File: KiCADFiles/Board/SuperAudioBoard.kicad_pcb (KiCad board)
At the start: 4 copper layers, 88.9 x 68.6 mm, 288 parts, among them K301 CONN_3, K302 CONN_3, K303 CONN_3, K304 CONN_3, K801 CONN_3, M3_HOLE VAL**, P801 CONN_2, U201 TEENSY_3_1, U202 SI8662BC, U203 SI8602AC, U301 CS4272, U302 OPA2348, U401 THS4521, U501 THS4521, U601 THS4521, U701 THS4521, U801 BAT4XAA, U802 LT1962-3.3, U803 LT1962-5, U804 LTC3534, X301 CRYSTAL

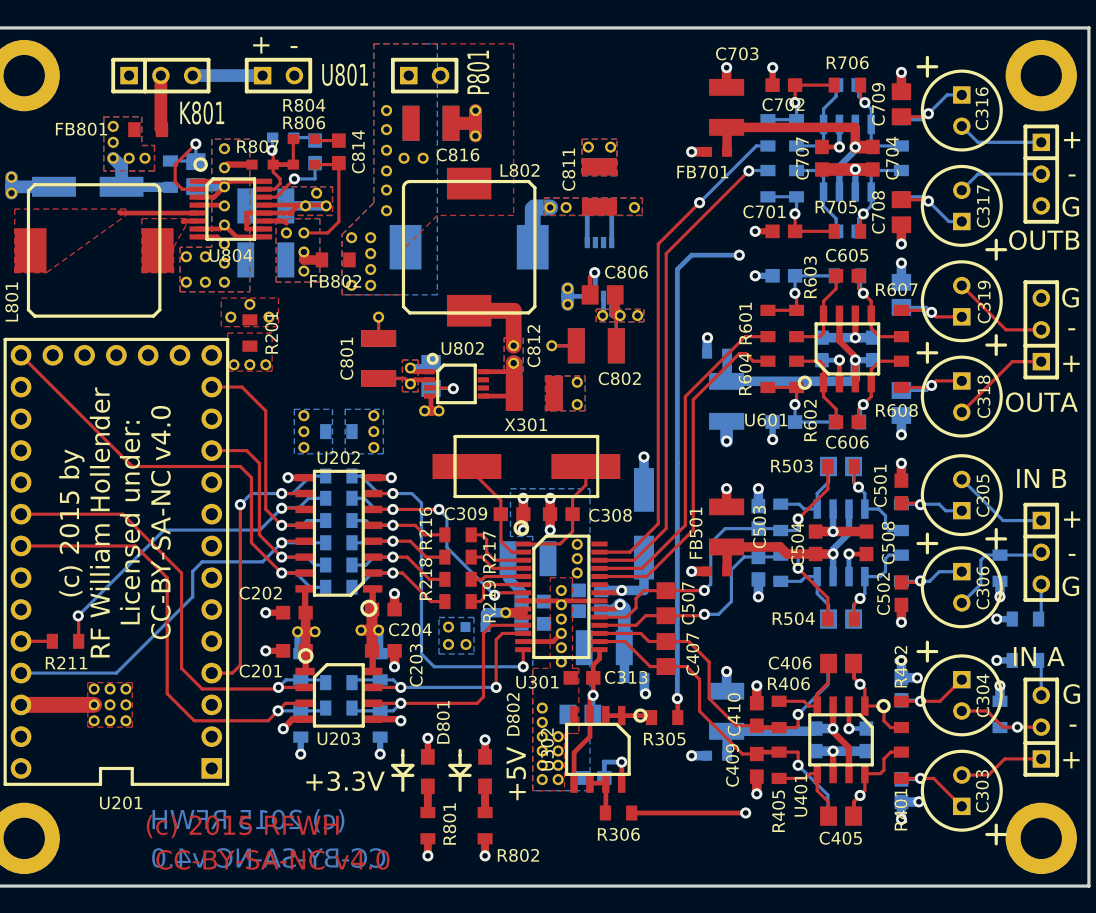
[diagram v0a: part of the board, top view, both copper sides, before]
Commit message: initial schematic with RPI pico
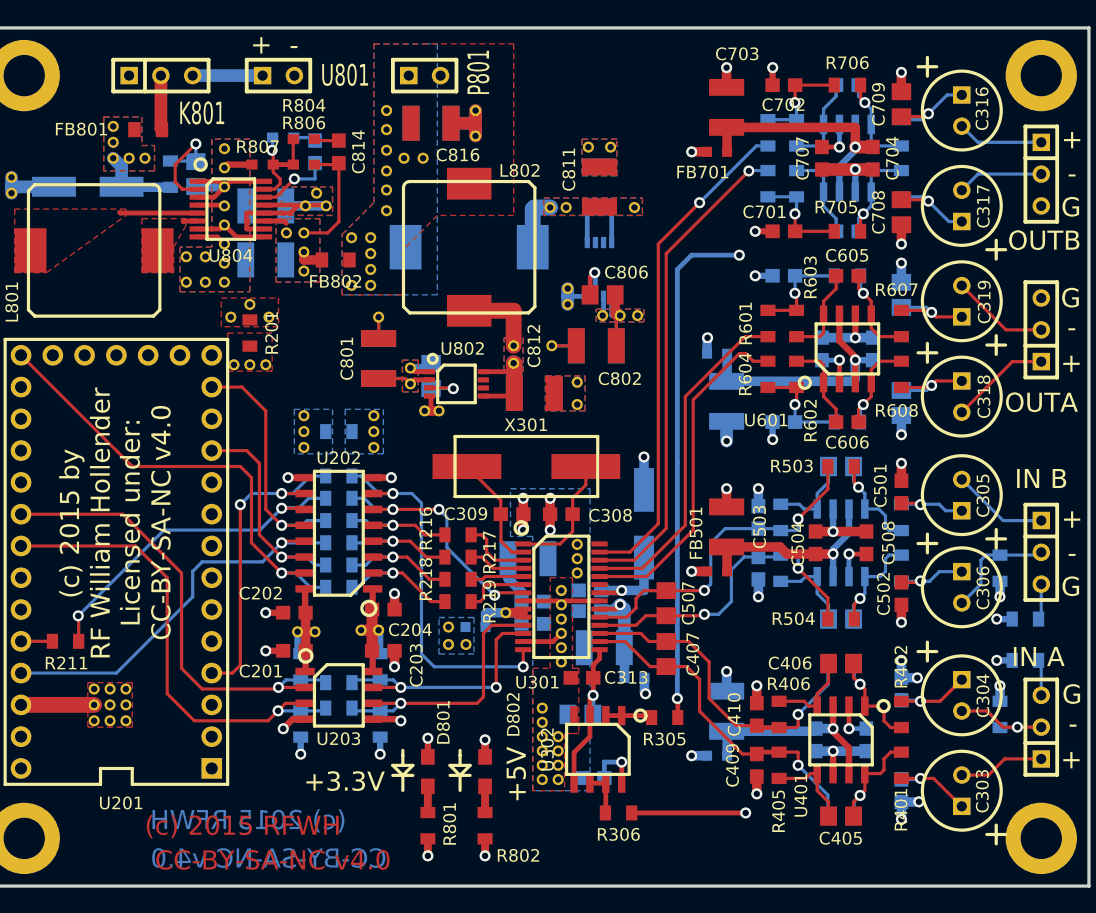
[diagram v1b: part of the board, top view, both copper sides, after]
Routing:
- added copper zone on In2.Cu, net +3.3V
- added copper zone on In2.Cu, net +5VA
- added copper zone on In2.Cu, net /TeensyAndDigital/T_3.3V
- added copper zone on In2.Cu, net /TeensyAndDigital/T_VIN
- added copper zone on In2.Cu, net /TeensyAndDigital/VUSB
- added copper zone on In1.Cu, net DGND
- added copper zone on In1.Cu, net GND
- added copper zone on In2.Cu, net GND
- added copper zone on In2.Cu, net N-00000104
- removed copper zone on Inner1.Cu, net +3.3V
- removed copper zone on Inner1.Cu, net +5VA
- removed copper zone on Inner1.Cu, net /TeensyAndDigital/T_3.3V
- removed copper zone on Inner1.Cu, net /TeensyAndDigital/T_VIN
- removed copper zone on Inner1.Cu, net /TeensyAndDigital/VUSB
- removed copper zone on Inner2.Cu, net DGND
- removed copper zone on Inner1.Cu, net GND
- removed copper zone on Inner2.Cu, net GND
- removed copper zone on Inner1.Cu, net N-00000104
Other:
- net class Default removed
- net class Thick1 removed
- net class Thick2 removed
- net class Thick3 removed
- net class Thick4 removed
- net class Thick5 removed

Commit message: chose all components
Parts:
- removed C201, C202, C203, C204, C301, C307, C312, C313, C314, C320, C404, C408, C504, C508, C604, C607, C704, C707: 0.1u, Kemet_0603
- removed C302, C310, C403, C503, C603, C703, C801, C802, C803, C804, C808, C810, C811, C812, C813, C816, C817: 10uF, Kemet_1210
- removed C303, C304, C305, C306, C316, C317, C318, C319: 100u, Nichicon_UFW_6_3mm
- removed C308, C309: 39p, Kemet_0603
- removed C311: 1u, Kemet_0805
- removed C315, C807: 47uF, Elec_cap_47u
- removed C401, C402, C409, C410, C501, C502, C509, C510: 100p, Kemet_0603
- removed C405, C406, C505, C506: 1n, Kemet_0805
- removed C407, C507: 2.7n, Kemet_0805
- removed C601, C602, C701, C702: 1.3nF, Kemet_0603
- removed C605, C606, C705, C706: 300pF, Kemet_0603
- removed C608, C609, C708, C709: 33nF, Kemet_0805
- removed C805, C806: 0.01uF, Kemet_0805
- removed C809: 0.056uF, Kemet_0805
- removed C814: 33pF, Kemet_0603
- removed C815: 330pF, Kemet_0603
- removed C818: 22uF, Kemet_1210
- removed D801, D802: LED, LED_0805
- removed FB301, FB302, FB401, FB501, FB601, FB701: 220, Bead_0603
- removed FB801, FB802: 330R, Bead_0805
- removed K301, K302, K303, K304, K801: CONN_3, SIL-3
- removed L801, L802, L803: 5.2uH, MSS1038
- removed M3_HOLE (x4): VAL**, M3_HOLE
- removed P801: CONN_2, SIL-2
- removed R201, R202, R203, R204, R205, R206, R207, R208, R209, R210, R301, R302, R303, R304: 0, Yageo_0805
- removed R211, R216, R217, R218, R219: 51, Yageo_0805
- removed R212, R213, R214, R215: 2.2K, Yageo_0805
- removed R305, R306: 10, Yageo_0805
- removed R401, R402, R403, R404, R501, R502, R503, R504: 1k, Yageo_0805
- removed R405, R406, R505, R506: 40.2, Yageo_0805
- removed R601, R602, R603, R604, R605, R606, R701, R702, R703, R704, R705, R706: 5.1K, Yageo_0805
- removed R607, R608, R707, R708: 100, Yageo_0805
- removed R801: 270, Yageo_0805
- removed R802: 620, Yageo_0805
- removed R803: 200k, Yageo_0805
- removed R804: 10k, Yageo_0603
- removed R805: 15k, Yageo_0603
- removed R806: 649k, Yageo_0603
- removed R807: 137k, Yageo_0603
- removed STITCHING_VIA (x111): VAL**, STITCHING_VIA
- removed U201: TEENSY_3_1, TEENSY_3_1
- removed U202: SI8662BC, SILABS_N_SOIC_16
- removed U203: SI8602AC, SILABS_N_SOIC_8
- removed U301: CS4272, INF_TSSOP_28
- removed U302: OPA2348, TI_SOIC8
- removed U401, U501, U601, U701: THS4521, TI_SOIC8
- removed U801: BAT4XAA, SIL-2
- removed U802: LT1962-3.3, LINEAR_MS8
- removed U803: LT1962-5, LINEAR_MS8
- removed U804: LTC3534, LINEAR_SSOP_16_N
- removed X301: CRYSTAL, XTAL
- added C14: 2200p, PCM_SparkFun-Capacitor:C_0603_1608Metric, F.Cu at (203.3, 136.5)
- added C15: 470p, PCM_SparkFun-Capacitor:C_0603_1608Metric, F.Cu at (129.9, 139.2)
- added C18: 100u, Capacitor_THT:CP_Radial_D5.0mm_P2.00mm, F.Cu at (161.1, 80.1)
- added C21: 100u, Capacitor_THT:CP_Radial_D5.0mm_P2.00mm, F.Cu at (161.1, 86.7)
- added C23: 100u, Capacitor_THT:CP_Radial_D5.0mm_P2.00mm, F.Cu at (161.1, 93.2)
- added C24: 470p, PCM_SparkFun-Capacitor:C_0603_1608Metric, F.Cu at (217.1, 103.1)
- added C34: 100u, Capacitor_THT:CP_Radial_D5.0mm_P2.00mm, F.Cu at (161.1, 99.8)
- added C39: 470p, PCM_SparkFun-Capacitor:C_0603_1608Metric, F.Cu at (217.1, 105.6)
- added C40: 0.1u, PCM_SparkFun-Capacitor:C_0603_1608Metric, F.Cu at (217.1, 108.1)
- added C41: 470p, PCM_SparkFun-Capacitor:C_0603_1608Metric, F.Cu at (203.3, 139.1)
- added C42: 1500p, PCM_SparkFun-Capacitor:C_0603_1608Metric, F.Cu at (129.9, 141.7)
- added C45: 1500p, PCM_SparkFun-Capacitor:C_0603_1608Metric, F.Cu at (203.3, 141.6)
- added C46: 22u, Capacitor_THT:CP_Radial_D5.0mm_P2.00mm, F.Cu at (134.2, 145.3)
- added C47: 22u, Capacitor_THT:CP_Radial_D5.0mm_P2.00mm, F.Cu at (207.7, 145.1)
- added C48: 6.8n, PCM_SparkFun-Capacitor:C_0603_1608Metric, F.Cu at (129.9, 144.2)
- added C49: 6.8n, PCM_SparkFun-Capacitor:C_0603_1608Metric, F.Cu at (203.3, 144.1)
- added C50: 10u, PCM_SparkFun-Capacitor:C_0805_2012Metric, F.Cu at (134.1, 150.1)
- added C51: 0.1u, PCM_SparkFun-Capacitor:C_0603_1608Metric, F.Cu at (129.9, 146.8)
- added C54: 10u, PCM_SparkFun-Capacitor:C_0805_2012Metric, F.Cu at (207.5, 149.9)
- added C55: 0.1u, PCM_SparkFun-Capacitor:C_0603_1608Metric, F.Cu at (203.3, 146.6)
- added C56: 100u, Capacitor_THT:CP_Radial_D5.0mm_P2.00mm, F.Cu at (161.1, 106.3)
- added C7: 100u, Capacitor_THT:CP_Radial_D5.0mm_P2.00mm, F.Cu at (211.7, 121.6)
- added C80: 0.1u, PCM_SparkFun-Capacitor:C_0603_1608Metric, F.Cu at (178.3, 132.3)
- added C81: 1n, PCM_SparkFun-Capacitor:C_0603_1608Metric, F.Cu at (178.3, 134.8)
- added C82: 1n, PCM_SparkFun-Capacitor:C_0603_1608Metric, F.Cu at (178.3, 137.3)
- added C85: 5800p, PCM_SparkFun-Capacitor:C_0603_1608Metric, F.Cu at (178.3, 139.8)
- added C86: 5800p, PCM_SparkFun-Capacitor:C_0603_1608Metric, F.Cu at (178.3, 142.3)
- added C9: 2200p, PCM_SparkFun-Capacitor:C_0603_1608Metric, F.Cu at (129.9, 136.7)
- added C90: 0.1u, PCM_SparkFun-Capacitor:C_0603_1608Metric, F.Cu at (211.1, 68.5)
- added C91: 1n, PCM_SparkFun-Capacitor:C_0603_1608Metric, F.Cu at (211.1, 71.0)
- added C92: 1n, PCM_SparkFun-Capacitor:C_0603_1608Metric, F.Cu at (211.1, 73.5)
- added C95: 5800p, PCM_SparkFun-Capacitor:C_0603_1608Metric, F.Cu at (211.1, 76.0)
- added C96: 5800p, PCM_SparkFun-Capacitor:C_0603_1608Metric, F.Cu at (211.1, 78.5)
- added FB7: 220, Inductor_SMD:L_0603_1608Metric, F.Cu at (129.9, 149.3)
- added FB8: 220, Inductor_SMD:L_0603_1608Metric, F.Cu at (203.3, 149.1)
- added J1: NCJ5FI-H, Connector_Audio:Jack_XLR-6.35mm_Neutrik_NCJ5FI-H_Horizontal, F.Cu at (167.8, 56.2)
- added J2: NRJ4HF, Connector_Audio:Jack_6.35mm_Neutrik_NRJ4HF_Horizontal, F.Cu at (131.8, 50.9)
- added J3: Barrel_Jack_PTH, PCM_SparkFun-Connector:Barrel_Jack_PTH, F.Cu at (202.0, 127.9)
- added J4: NRJ4HF, Connector_Audio:Jack_6.35mm_Neutrik_NRJ4HF_Horizontal, F.Cu at (131.8, 68.7)
- added J5: NRJ4HF, Connector_Audio:Jack_6.35mm_Neutrik_NRJ4HF_Horizontal, F.Cu at (131.8, 86.5)
- added R10: 5, PCM_SparkFun-Resistor:R_0805_2012Metric, F.Cu at (225.5, 89.8)
- added R11: 1k, PCM_SparkFun-Resistor:R_0805_2012Metric, F.Cu at (225.5, 92.7)
- added R12: 100, PCM_SparkFun-Resistor:R_0805_2012Metric, F.Cu at (167.5, 81.3)
- added R14: 1k, PCM_SparkFun-Resistor:R_0805_2012Metric, F.Cu at (165.6, 116.0)
- added R15: 1k, PCM_SparkFun-Resistor:R_0805_2012Metric, F.Cu at (198.5, 52.2)
- added R16: 39k, PCM_SparkFun-Resistor:R_0805_2012Metric, F.Cu at (225.5, 95.7)
- added R17: 1k, PCM_SparkFun-Resistor:R_0805_2012Metric, F.Cu at (225.5, 98.6)
- added R18: 4.42k, PCM_SparkFun-Resistor:R_0805_2012Metric, F.Cu at (125.7, 136.9)
- added R19: 4.42k, PCM_SparkFun-Resistor:R_0805_2012Metric, F.Cu at (199.1, 136.8)
- added R20: 1.33k, PCM_SparkFun-Resistor:R_0805_2012Metric, F.Cu at (125.7, 139.9)
- added R21: 1.33k, PCM_SparkFun-Resistor:R_0805_2012Metric, F.Cu at (199.1, 139.7)
- added R22: 2.32k, PCM_SparkFun-Resistor:R_0805_2012Metric, F.Cu at (125.7, 142.8)
- added R23: 715, PCM_SparkFun-Resistor:R_0805_2012Metric, F.Cu at (125.7, 145.8)
- added R24: 2.32k, PCM_SparkFun-Resistor:R_0805_2012Metric, F.Cu at (199.1, 142.7)
- added R25: 715, PCM_SparkFun-Resistor:R_0805_2012Metric, F.Cu at (199.1, 145.6)
- added R26: 4.99k, PCM_SparkFun-Resistor:R_0805_2012Metric, F.Cu at (125.7, 148.7)
- added R27: 4.99k, PCM_SparkFun-Resistor:R_0805_2012Metric, F.Cu at (199.1, 148.6)
- added R28: 1.5k, PCM_SparkFun-Resistor:R_0805_2012Metric, F.Cu at (125.7, 151.7)
- added R29: 1.5k, PCM_SparkFun-Resistor:R_0805_2012Metric, F.Cu at (199.1, 151.5)
- added R3: 39k, PCM_SparkFun-Resistor:R_0805_2012Metric, F.Cu at (211.6, 126.3)
- added R30: 100, PCM_SparkFun-Resistor:R_0805_2012Metric, F.Cu at (167.5, 84.2)
- added R31: 100, PCM_SparkFun-Resistor:R_0805_2012Metric, F.Cu at (167.5, 87.2)
- added R32: 47k, PCM_SparkFun-Resistor:R_0805_2012Metric, F.Cu at (167.5, 90.1)
- added R33: 47k, PCM_SparkFun-Resistor:R_0805_2012Metric, F.Cu at (167.5, 93.1)
- added R34: 100, PCM_SparkFun-Resistor:R_0805_2012Metric, F.Cu at (167.5, 96.0)
- added R35: 0, PCM_SparkFun-Resistor:R_0805_2012Metric, F.Cu at (125.7, 132.0)
- added R4: 3.3k, PCM_SparkFun-Resistor:R_0805_2012Metric, F.Cu at (211.6, 129.3)
- added R5: 39k, PCM_SparkFun-Resistor:R_0805_2012Metric, F.Cu at (167.5, 78.3)
- added R6: 34, PCM_SparkFun-Resistor:R_0805_2012Metric, F.Cu at (225.5, 83.9)
- added R65: 10k, PCM_SparkFun-Resistor:R_0805_2012Metric, F.Cu at (165.6, 119.0)
- added R67: 1k, PCM_SparkFun-Resistor:R_0805_2012Metric, F.Cu at (165.6, 121.9)
- added R69: 1k, PCM_SparkFun-Resistor:R_0805_2012Metric, F.Cu at (165.6, 124.9)
- added R7: 39k, PCM_SparkFun-Resistor:R_0805_2012Metric, F.Cu at (225.5, 86.8)
- added R70: 34, PCM_SparkFun-Resistor:R_0805_2012Metric, F.Cu at (165.6, 127.8)
- added R71: 34, PCM_SparkFun-Resistor:R_0805_2012Metric, F.Cu at (165.6, 130.8)
- added R74: 10k, PCM_SparkFun-Resistor:R_0805_2012Metric, F.Cu at (198.5, 55.2)
- added R76: 1k, PCM_SparkFun-Resistor:R_0805_2012Metric, F.Cu at (198.5, 58.1)
- added R78: 1k, PCM_SparkFun-Resistor:R_0805_2012Metric, F.Cu at (198.5, 61.1)
- added R79: 34, PCM_SparkFun-Resistor:R_0805_2012Metric, F.Cu at (198.5, 64.0)
- added R8: 500, PCM_SparkFun-Resistor:R_0805_2012Metric, F.Cu at (165.6, 113.1)
- added R80: 34, PCM_SparkFun-Resistor:R_0805_2012Metric, F.Cu at (198.5, 67.0)
- added R9: 500, PCM_SparkFun-Resistor:R_0805_2012Metric, F.Cu at (198.5, 49.3)
- added RV3: 5k, Potentiometer_THT:Potentiometer_Alps_RK163_Single_Horizontal, F.Cu at (215.8, 87.1)
- added RV4: 5k, Potentiometer_THT:Potentiometer_Alps_RK163_Single_Horizontal, F.Cu at (187.4, 116.3)
- added RV5: 5k, Potentiometer_THT:Potentiometer_Alps_RK163_Single_Horizontal, F.Cu at (220.2, 52.5)
- added SW4: ~, Connector_PinHeader_2.54mm:PinHeader_1x03_P2.54mm_Horizontal, F.Cu at (178.2, 79.1)
- added TP1: TestPoint_2Pole, TestPoint:TestPoint_2Pads_Pitch2.54mm_Drill0.8mm, F.Cu at (211.2, 113.3)
- added TP2: TestPoint_2Pole, TestPoint:TestPoint_2Pads_Pitch2.54mm_Drill0.8mm, F.Cu at (211.2, 116.6)
- added TP3: TestPoint_2Pole, TestPoint:TestPoint_2Pads_Pitch2.54mm_Drill0.8mm, F.Cu at (171.6, 78.5)
- added TP4: TestPoint_2Pole, TestPoint:TestPoint_2Pads_Pitch2.54mm_Drill0.8mm, F.Cu at (171.6, 81.9)
- added TP5: TestPoint_2Pole, TestPoint:TestPoint_2Pads_Pitch2.54mm_Drill0.8mm, F.Cu at (171.6, 85.2)
- added TP6: TestPoint_2Pole, TestPoint:TestPoint_2Pads_Pitch2.54mm_Drill0.8mm, F.Cu at (171.6, 88.6)
- added U1: OPA1655D, Package_SO:SOIC-8_3.9x4.9mm_P1.27mm, F.Cu at (136.1, 138.8)
- added U10: OPA1655D, Package_SO:SOIC-8_3.9x4.9mm_P1.27mm, F.Cu at (210.8, 105.2)
- added U15: OPA1655D, Package_SO:SOIC-8_3.9x4.9mm_P1.27mm, F.Cu at (172.1, 134.4)
- added U16: OPA1655D, Package_SO:SOIC-8_3.9x4.9mm_P1.27mm, F.Cu at (172.1, 141.0)
- added U17: OPA1655D, Package_SO:SOIC-8_3.9x4.9mm_P1.27mm, F.Cu at (204.9, 70.6)
- added U18: OPA1655D, Package_SO:SOIC-8_3.9x4.9mm_P1.27mm, F.Cu at (204.9, 77.2)
- added U4: OPA1655D, Package_SO:SOIC-8_3.9x4.9mm_P1.27mm, F.Cu at (209.5, 138.6)
- added U6: 1512S08-U, Package_SO:SOIC-8_5.3x5.3mm_P1.27mm, F.Cu at (201.4, 105.4)
- added U7: Teensy4.0, Teensy:Teensy40, F.Cu at (143.1, 121.0)
- added U8: LT1962, Package_SO:MSOP-8_3x3mm_P0.65mm, F.Cu at (200.6, 131.0)
- added U9: OPA1655D, Package_SO:SOIC-8_3.9x4.9mm_P1.27mm, F.Cu at (174.0, 93.6)
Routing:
- net GND: track 135.0 -> 0.00 mm, vias 41 -> 0
- net /CodecAndAnalog/OutputBufferA/VCOM: track 72.7 -> 0.00 mm, vias 4 -> 0
- net /CodecAndAnalog/InputBufferA/VCOM: track 58.0 -> 0.00 mm, vias 3 -> 0
- net /CodecAndAnalog/OutputBufferB/IN_N: track 40.0 -> 0.00 mm, vias 1 -> 0
- net /CodecAndAnalog/OutputBufferB/IN_P: track 39.2 -> 0.00 mm, vias 1 -> 0
- net /TeensyAndDigital/T_SCL: track 38.4 -> 0.00 mm, vias 1 -> 0
- net /TeensyAndDigital/T_SDA: track 37.1 -> 0.00 mm, vias 1 -> 0
- net /TeensyAndDigital/T_ADC_DATA: track 37.0 -> 0.00 mm, vias 1 -> 0
- net /TeensyAndDigital/T_LRCLK: track 31.8 -> 0.00 mm, vias 1 -> 0
- net /TeensyAndDigital/RSTN: track 30.0 -> 0.00 mm, vias 2 -> 0
- net /TeensyAndDigital/T_DAC_DATA: track 27.6 -> 0.00 mm, vias 2 -> 0
- net /CodecAndAnalog/InputBufferB/OUT_N: track 27.3 -> 0.00 mm, vias 2 -> 0
- net /CodecAndAnalog/InputBufferA/OUT_N: track 27.2 -> 0.00 mm, vias 1 -> 0
- net /CodecAndAnalog/OutputBufferA/IN_N: track 27.2 -> 0.00 mm
- net /CodecAndAnalog/OutputBufferA/IN_P: track 27.2 -> 0.00 mm
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- removed copper zone on B.Cu, net +3.3V
- removed copper zone on F.Cu, net +3.3V
- removed copper zone on In2.Cu, net +3.3V
- removed copper zone on B.Cu, net +5VA
- removed copper zone on F.Cu, net +5VA
- removed copper zone on In2.Cu, net +5VA
- removed copper zone on F.Cu, net /TeensyAndDigital/T_3.3V
- removed copper zone on In2.Cu, net /TeensyAndDigital/T_3.3V
- removed copper zone on F.Cu, net /TeensyAndDigital/T_VIN
- removed copper zone on In2.Cu, net /TeensyAndDigital/T_VIN
- removed copper zone on F.Cu, net /TeensyAndDigital/VUSB
- removed copper zone on In2.Cu, net /TeensyAndDigital/VUSB
- removed copper zone on B.Cu, net DGND
- removed copper zone on In1.Cu, net DGND
- removed copper zone on B.Cu, net GND
- removed copper zone on F.Cu, net GND
- removed copper zone on In1.Cu, net GND
- removed copper zone on In2.Cu, net GND
- removed copper zone on B.Cu, net N-00000101
- removed copper zone on F.Cu, net N-00000101
- removed copper zone on B.Cu, net N-00000104
- removed copper zone on F.Cu, net N-00000104
- removed copper zone on In2.Cu, net N-00000104
- removed copper zone on F.Cu, net N-00000107
- removed copper zone on F.Cu, net N-00000110
- removed copper zone on B.Cu, net N-0000091
- removed copper zone on F.Cu, net N-0000091
- removed copper zone on B.Cu, net N-0000096
- removed copper zone on F.Cu, net N-0000096
- removed copper zone on B.Cu, net N-0000098
- removed copper zone on F.Cu, net N-0000098
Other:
- board outline removed
- board text removed: "(c) 2015 RFWH"
- board text removed: "CC-BY-SA-NC v4.0"

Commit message: replaced sw with relay, routed line amp section
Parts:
- removed SW4: ~, Connector_PinHeader_2.54mm:PinHeader_1x03_P2.54mm_Horizontal
- added C1: 10u, PCM_SparkFun-Capacitor:C_0805_2012Metric, F.Cu at (212.5, 68.2)
- added C10: 10u, PCM_SparkFun-Capacitor:C_0805_2012Metric, F.Cu at (229.0, 70.5)
- added C11: 10u, PCM_SparkFun-Capacitor:C_0805_2012Metric, F.Cu at (230.0, 82.0)
- added C12: 10u, PCM_SparkFun-Capacitor:C_0805_2012Metric, F.Cu at (232.0, 70.5)
- added C13: 10u, PCM_SparkFun-Capacitor:C_0805_2012Metric, F.Cu at (233.0, 82.0)
- added C16: 10u, PCM_SparkFun-Capacitor:C_0805_2012Metric, F.Cu at (237.5, 70.5)
- added C17: 10u, PCM_SparkFun-Capacitor:C_0805_2012Metric, F.Cu at (240.2, 70.5)
- added C19: 0.1u, PCM_SparkFun-Capacitor:C_0603_1608Metric, F.Cu at (123.1, 73.5)
- added C2: 10u, PCM_SparkFun-Capacitor:C_0805_2012Metric, F.Cu at (216.8, 79.5)
- added C20: 10u, PCM_SparkFun-Capacitor:C_0805_2012Metric, F.Cu at (137.9, 85.1)
- added C22: 0.1u, PCM_SparkFun-Capacitor:C_0603_1608Metric, F.Cu at (216.3, 105.7)
- added C25: 0.1u, PCM_SparkFun-Capacitor:C_0603_1608Metric, F.Cu at (123.1, 76.0)
- added C26: 39p, PCM_SparkFun-Capacitor:C_0603_1608Metric, F.Cu at (123.1, 78.5)
- added C27: 39p, PCM_SparkFun-Capacitor:C_0603_1608Metric, F.Cu at (123.1, 81.0)
- added C28: 10u, PCM_SparkFun-Capacitor:C_0805_2012Metric, F.Cu at (137.9, 88.1)
- added C29: 1u, PCM_SparkFun-Capacitor:C_0603_1608Metric, F.Cu at (123.1, 83.5)
- added C3: 10u, PCM_SparkFun-Capacitor:C_0805_2012Metric, F.Cu at (215.2, 68.2)
- added C30: 0.1u, PCM_SparkFun-Capacitor:C_0603_1608Metric, F.Cu at (123.1, 86.0)
- added C31: 0.1u, PCM_SparkFun-Capacitor:C_0603_1608Metric, F.Cu at (127.1, 73.5)
- added C32: 0.1u, PCM_SparkFun-Capacitor:C_0603_1608Metric, F.Cu at (127.1, 76.0)
- added C33: 0.1u, PCM_SparkFun-Capacitor:C_0603_1608Metric, F.Cu at (151.2, 105.7)
- added C35: 0.1u, PCM_SparkFun-Capacitor:C_0603_1608Metric, F.Cu at (185.5, 99.0)
- added C36: 0.1u, PCM_SparkFun-Capacitor:C_0603_1608Metric, F.Cu at (151.2, 108.2)
- added C37: 0.1u, PCM_SparkFun-Capacitor:C_0603_1608Metric, F.Cu at (185.2, 108.8)
- added C38: 0.1u, PCM_SparkFun-Capacitor:C_0603_1608Metric, F.Cu at (151.2, 77.8)
- added C4: 10u, PCM_SparkFun-Capacitor:C_0805_2012Metric, F.Cu at (213.8, 79.5)
- added C43: 10u, PCM_SparkFun-Capacitor:C_0805_2012Metric, F.Cu at (153.0, 89.0)
- added C5: 0.01uF, PCM_SparkFun-Capacitor:C_0603_1608Metric, F.Cu at (218.2, 68.2)
- added C52: 10u, PCM_SparkFun-Capacitor:C_0805_2012Metric, F.Cu at (183.0, 99.2)
- added C6: 0.01uF, PCM_SparkFun-Capacitor:C_0603_1608Metric, F.Cu at (219.8, 79.8)
- added C75: 0.1u, PCM_SparkFun-Capacitor:C_0603_1608Metric, F.Cu at (-6.38, 182.8)
- added C76: 0.1u, PCM_SparkFun-Capacitor:C_0603_1608Metric, F.Cu at (-6.38, 185.3)
- added C77: 0.1u, PCM_SparkFun-Capacitor:C_0603_1608Metric, F.Cu at (-6.38, 187.8)
- added C78: 0.1u, PCM_SparkFun-Capacitor:C_0603_1608Metric, F.Cu at (-6.38, 190.3)
- added C8: 10u, PCM_SparkFun-Capacitor:C_0805_2012Metric, F.Cu at (252.4, 75.2)
- added D1: LED, LED_SMD:LED_0805_2012Metric, F.Cu at (208.5, 68.2)
- added D2: LED, LED_SMD:LED_0805_2012Metric, F.Cu at (209.8, 79.5)
- added FB1: 330, Inductor_SMD:L_0805_2012Metric, F.Cu at (249.2, 70.1)
- added FB2: 330, Inductor_SMD:L_0805_2012Metric, F.Cu at (243.8, 71.5)
- added FB3: 220, Inductor_SMD:L_0603_1608Metric, F.Cu at (127.1, 81.0)
- added FB4: 220, Inductor_SMD:L_0603_1608Metric, F.Cu at (127.1, 83.5)
- added FB5: 220, Inductor_SMD:L_0603_1608Metric, F.Cu at (152.8, 94.2)
- added FB6: 220, Inductor_SMD:L_0603_1608Metric, F.Cu at (179.8, 98.2)
- added K2: Fujitsu_FTR-LYCA005x, Relay_THT:Relay_SPDT_Fujitsu_FTR-LYCA005x_FormC_Vertical, F.Cu at (209.3, 117.6)
- added L2: 6.8uH, Inductor_SMD:L_0805_2012Metric, F.Cu at (230.0, 66.5)
- added L3: 6.8uH, Inductor_SMD:L_0805_2012Metric, F.Cu at (231.0, 78.0)
- added R1: 3.3k, PCM_SparkFun-Resistor:R_0805_2012Metric, F.Cu at (208.5, 72.2)
- added R13: 34, PCM_SparkFun-Resistor:R_0805_2012Metric, F.Cu at (147.0, 78.0)
- added R2: 3.3k, PCM_SparkFun-Resistor:R_0805_2012Metric, F.Cu at (209.8, 83.8)
- added R36: 100, PCM_SparkFun-Resistor:R_0805_2012Metric, F.Cu at (204.8, 106.0)
- added R37: 100, PCM_SparkFun-Resistor:R_0805_2012Metric, F.Cu at (204.8, 108.5)
- added R46: 0, PCM_SparkFun-Resistor:R_0805_2012Metric, F.Cu at (-19.4, 171.1)
- added R47: 0, PCM_SparkFun-Resistor:R_0805_2012Metric, F.Cu at (-19.4, 174.0)
- added R48: 0, PCM_SparkFun-Resistor:R_0805_2012Metric, F.Cu at (-19.4, 176.9)
- added R49: 0, PCM_SparkFun-Resistor:R_0805_2012Metric, F.Cu at (-19.4, 179.9)
- added R50: 0, PCM_SparkFun-Resistor:R_0805_2012Metric, F.Cu at (-19.4, 182.8)
- added R51: 0, PCM_SparkFun-Resistor:R_0805_2012Metric, F.Cu at (-19.4, 185.8)
- added R52: 0, PCM_SparkFun-Resistor:R_0805_2012Metric, F.Cu at (-19.4, 188.8)
- added R53: 0, PCM_SparkFun-Resistor:R_0805_2012Metric, F.Cu at (-15.0, 171.1)
- added R54: 0, PCM_SparkFun-Resistor:R_0805_2012Metric, F.Cu at (-15.0, 174.0)
- added R55: 0, PCM_SparkFun-Resistor:R_0805_2012Metric, F.Cu at (-15.0, 176.9)
- added R56: 51, PCM_SparkFun-Resistor:R_0805_2012Metric, F.Cu at (-15.0, 179.9)
- added R57: 2.2K, PCM_SparkFun-Resistor:R_0805_2012Metric, F.Cu at (-15.0, 182.8)
- added R58: 2.2K, PCM_SparkFun-Resistor:R_0805_2012Metric, F.Cu at (-15.0, 185.8)
- added R59: 2.2K, PCM_SparkFun-Resistor:R_0805_2012Metric, F.Cu at (-15.0, 188.8)
- added R60: 2.2K, PCM_SparkFun-Resistor:R_0805_2012Metric, F.Cu at (-10.6, 171.1)
- added R61: 51, PCM_SparkFun-Resistor:R_0805_2012Metric, F.Cu at (-10.6, 174.0)
- added R62: 51, PCM_SparkFun-Resistor:R_0805_2012Metric, F.Cu at (-10.6, 176.9)
- added R63: 51, PCM_SparkFun-Resistor:R_0805_2012Metric, F.Cu at (-10.6, 179.9)
- added R64: 51, PCM_SparkFun-Resistor:R_0805_2012Metric, F.Cu at (-10.6, 182.8)
- added TP7: TestPoint_2Pole, TestPoint:TestPoint_2Pads_Pitch2.54mm_Drill0.8mm, F.Cu at (202.0, 112.5)
- added U13: SI8662BC, Package_SO:SOIC-16W_7.5x10.3mm_P1.27mm, F.Cu at (-1.93, 175.6)
- added U14: SI8602AC, Package_SO:SOIC-8_3.9x4.9mm_P1.27mm, F.Cu at (-0.15, 184.9)
- added U2: LT1962-3.3, Package_SO:MSOP-8_3x3mm_P0.65mm, F.Cu at (223.0, 67.5)
- added U3: LT1962-5, Package_SO:MSOP-8_3x3mm_P0.65mm, F.Cu at (224.5, 79.0)
- added U5: CS4272, Package_SO:TSSOP-28-1EP_4.4x9.7mm_P0.65mm_EP2.74x4.75mm, F.Cu at (133.4, 77.9)
- added X1: 24.576 MHz 20 pF, Crystal:Crystal_SMD_3225-4Pin_3.2x2.5mm_HandSoldering, F.Cu at (132.4, 86.4)
- C15, C24, C39, C41: footprint PCM_SparkFun-Capacitor:C_0603_1608Metric -> PCM_SparkFun-Capacitor:C_0805_2012Metric
- R5: value 39k -> 1M
- moved R35 175.9 mm to (-50.1, 137.3)
- moved C18 175.9 mm to (-14.7, 85.4)
- moved C21 175.9 mm to (-14.7, 92.0)
- moved C34 175.9 mm to (-14.7, 105.1)
- moved C56 175.9 mm to (-14.7, 111.6)
- moved R12 175.9 mm to (-8.23, 86.6)
- moved R30 175.9 mm to (-8.23, 89.5)
- moved R31 175.9 mm to (-8.23, 92.5)
- moved R32 175.9 mm to (-8.23, 95.4)
- moved R33 175.9 mm to (-8.23, 98.4)
- moved TP3 175.9 mm to (-4.20, 83.8)
- moved TP4 175.9 mm to (-4.20, 87.2)
- moved TP5 175.9 mm to (-4.20, 90.5)
- moved TP6 175.9 mm to (-4.20, 93.9)
- moved C14 141.1 mm to (94.9, 46.2)
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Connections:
- net Net-(J3-PWR) renamed /PowerSupply/VIN_ANALOG
- net Net-(U8-IN) renamed /PowerSupply/VIN_ANALOG_FILT
- R3 pad 1: +15V -> Net-(U8-OUT)
- RV3 pad 2: Net-(R10-Pad2) -> /CodecAndAnalog/MicPreamp/Rg-
- TP2 pad 2: Net-(C16-Pad1) -> +15V
- U8 pad 1: +15V -> Net-(U8-OUT)
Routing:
- net Net-(J1-PadT): track 0.00 -> 38.4 mm
- net GNDPWR: track 0.00 -> 33.4 mm
- net /CodecAndAnalog/InputBufferB/AMP_SIGIN+: track 0.00 -> 30.4 mm
- net /CodecAndAnalog/MicPreamp/IN_N: track 0.00 -> 29.6 mm
- net /CodecAndAnalog/MicPreamp/IN_P: track 0.00 -> 22.1 mm
- net /CodecAndAnalog/MicPreamp/Rg-: track 0.00 -> 21.7 mm
- net Net-(R9-Pad1): track 0.00 -> 20.9 mm
- net /CodecAndAnalog/MicPreamp/Vmid: track 0.00 -> 19.1 mm
- net /CodecAndAnalog/MicPreamp/OUT: track 0.00 -> 15.2 mm
- net /CodecAndAnalog/InputBufferB/AMP_SIGIN-: track 0.00 -> 13.7 mm
- net /CodecAndAnalog/InputBufferA/VCOM: track 0.00 -> 13.6 mm
- net /CodecAndAnalog/InputBufferB/VSIGIN: track 0.00 -> 12.2 mm
- net Net-(C91-Pad2): track 0.00 -> 11.1 mm
- net Net-(R10-Pad2): track 0.00 -> 10.5 mm
- net /CodecAndAnalog/REL_CTRL: track 0.00 -> 9.35 mm
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- added copper zone on B.Cu, net GND
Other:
- copper layers 4 -> 2
- board text added: "Use mounting lug for chassis ground"
- board text removed: "K801 is switching reg input select. Do not use Teensy Vusb input unless not isolated."
- board text removed: "P801 can be used to bypass the switching regulator if supply >6V is available. Linear regs can handle 20V inputs, but practical limit is approx 15V due to power dissipation."
- board text removed: "Teensy Vin selected"
- board text removed: "U801 is normal power supply input. Can accept 3V < Vin < 7V."
- board text removed: "U801 selected (default)"

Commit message: removed connectors and condensed layout
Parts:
- removed TP3, TP4, TP5, TP6, TP7: TestPoint_2Pole, TestPoint:TestPoint_2Pads_Pitch2.54mm_Drill0.8mm
- added J6: MONO JACK, Connector_PinHeader_2.54mm:PinHeader_1x02_P2.54mm_Vertical, F.Cu at (207.2, 41.5)
- added J7: MONO JACK, Connector_PinHeader_2.54mm:PinHeader_1x02_P2.54mm_Vertical, F.Cu at (204.8, 116.8)
- J1: value NCJ5FI-H -> XLR; footprint Connector_Audio:Jack_XLR-6.35mm_Neutrik_NCJ5FI-H_Horizontal -> Connector_PinHeader_2.54mm:PinHeader_1x03_P2.54mm_Vertical
- J2, J4, J5: value NRJ4HF -> MONO JACK; footprint Connector_Audio:Jack_6.35mm_Neutrik_NRJ4HF_Horizontal -> Connector_PinHeader_2.54mm:PinHeader_1x02_P2.54mm_Vertical
- moved C21 191.3 mm to (176.3, 102.5)
- moved R12 189.5 mm to (180.0, 108.2), turned to 180 degrees
- moved C76 188.2 mm to (150.7, 81.7)
- moved C77 188.2 mm to (150.7, 84.2)
- moved R46 188.2 mm to (137.7, 67.4)
- moved R47 188.2 mm to (137.7, 70.3)
- moved R49 188.2 mm to (137.7, 76.2)
- moved R51 188.2 mm to (137.7, 82.2)
- moved R52 188.2 mm to (137.7, 85.1)
- moved R53 188.2 mm to (142.1, 67.4)
- moved R54 188.2 mm to (142.1, 70.3)
- moved R56 188.2 mm to (142.1, 76.2)
- moved R58 188.2 mm to (142.1, 82.2)
- moved R59 188.2 mm to (142.1, 85.1)
- moved R60 188.2 mm to (146.5, 67.4)
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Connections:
- J1 pad 1: GNDPWR -> /CodecAndAnalog/MicPreamp/IN_P
- J1 pad 2: /CodecAndAnalog/MicPreamp/IN_P -> /CodecAndAnalog/MicPreamp/IN_N
- J1 pad 3: /CodecAndAnalog/MicPreamp/IN_N -> GNDPWR
- K2 pad 14: Net-(J1-PadT) -> Net-(J2-Pin_1)
- R12 pad 1: Net-(J2-PadT) -> Net-(J4-Pin_1)
- R30 pad 2: Net-(J4-PadT) -> Net-(J5-Pin_1)
- R31 pad 2: Net-(J5-PadT) -> Net-(J6-Pin_1)
- R32 pad 2: Net-(J4-PadT) -> Net-(J5-Pin_1)
- R33 pad 2: Net-(J5-PadT) -> Net-(J6-Pin_1)
- R8 pad 2: Net-(C81-Pad2) -> /CodecAndAnalog/InputBufferA/OUT_N
- R9 pad 2: Net-(C91-Pad2) -> /CodecAndAnalog/InputBufferB/OUT_N
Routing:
- net +15V: track 0.00 -> 42.4 mm, vias 0 -> 2
- net Net-(J1-PadT): track 38.4 -> 0.00 mm
- net GNDPWR: track 33.4 -> 8.86 mm
- net /CodecAndAnalog/InputBufferA/VCOM: track 13.6 -> 38.1 mm
- net /CodecAndAnalog/InputBufferA/5V_FILT: track 0.00 -> 23.0 mm
- net /CodecAndAnalog/InputBufferB/5V_FILT: track 0.00 -> 23.0 mm
- net /CodecAndAnalog/InputBufferA/AMP_SIGIN+: track 0.00 -> 19.8 mm
- net Net-(R8-Pad1): track 0.00 -> 15.4 mm
- net /CodecAndAnalog/MicPreamp/IN_N: track 29.6 -> 14.5 mm
- net /CodecAndAnalog/InputBufferA/AMP_SIGIN-: track 0.00 -> 14.0 mm
- net Net-(C81-Pad2): track 0.00 -> 11.5 mm
- net /CodecAndAnalog/InputBufferA/VSIGIN: track 0.00 -> 11.2 mm
- net Net-(U9--): track 0.00 -> 10.7 mm
- net Net-(C82-Pad2): track 0.00 -> 7.37 mm
- net /CodecAndAnalog/MicPreamp/IN_P: track 22.1 -> 15.4 mm
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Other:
- board outline added: 144.5 x 89.2 mm
- board text removed: "+3.3V"
- board text removed: "+5V"
- board text removed: "OUTA"
- board text removed: "OUTB"
